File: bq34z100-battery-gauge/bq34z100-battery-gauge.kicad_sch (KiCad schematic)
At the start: 78 parts, among them J1 Conn_01x04, J10 Conn_01x10, J11 LED, J2 ALERT, J3 NTC, J4 LED_DISP, J5 BAT, J6 BAT, J7 LOAD, J8 LOAD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

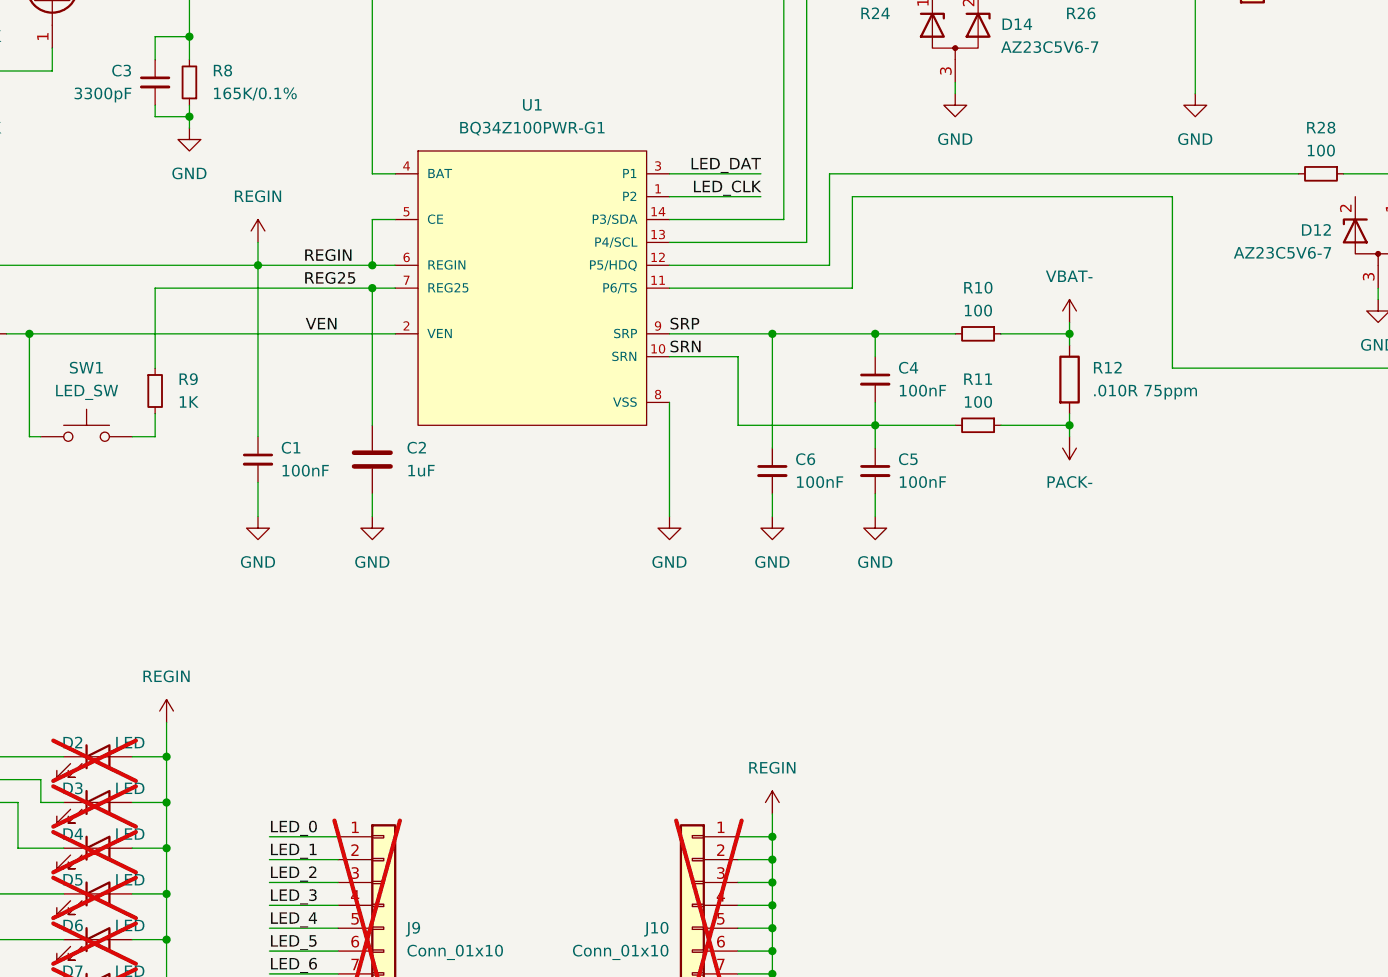
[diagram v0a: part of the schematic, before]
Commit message: Change Resistor to issabelenhurt, change mounting hole dimension
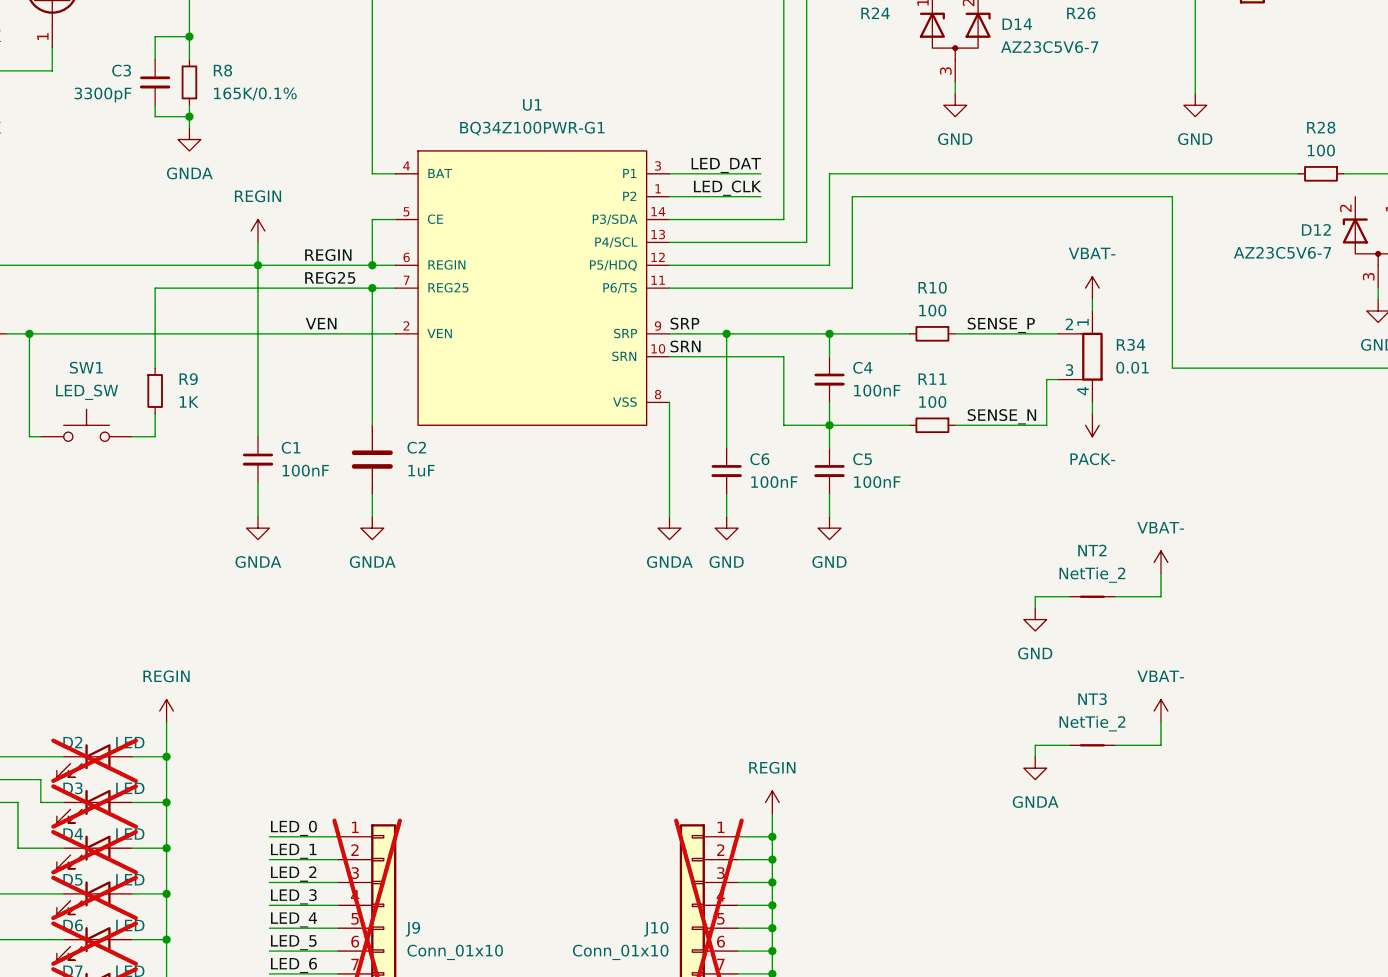
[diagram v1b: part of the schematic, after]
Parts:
- removed R12: .010R 75ppm, Resistor_SMD:R_2512_6332Metric, symbol Device:R
- added NT2, NT3: NetTie_2, NetTie:NetTie-2_SMD_Pad0.5mm, symbol Device:NetTie_2
- added R34: 0.01, shunt-resistor:Isabellenhuette-SMT-R010-1.0, symbol Device:R_Shunt
- J5, J6, J7, J8: footprint TerminalBlock_Wuerth:Wuerth_REDCUBE-THR_WP-THRBU_74650174_THR -> Plugin_terminal:square_terminal
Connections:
- net GND: now also NT2.1; no longer C1.2, C2.2, C3.2, R8.1, U1.8 (VSS)
- net PACK-: now also R34.4; no longer R11.1
- net VBAT-: now also NT2.2, NT3.2, R34.1; no longer R10.1
- new net GNDA: C1.2, C2.2, C3.2, NT3.1, R8.1, U1.8 (VSS)
- new net SENSE_N: R11.1, R34.3
- new net SENSE_P: R10.1, R34.2
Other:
- moved on the sheet: C4, C5, C6, R10, R11

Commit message: 1. Finished tracks, (need to verify grounding layer below battery tracks). 2. Added more literature document
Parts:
- removed R29: 1K, Resistor_SMD:R_0603_1608Metric, symbol Device:R_Small
- added TP1, TP2: TestPoint, TestPoint:TestPoint_Pad_D1.0mm, symbol Connector:TestPoint
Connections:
- net SENSE_N: now also TP2.1
- net SENSE_P: now also TP1.1
- net VEN: now also J4.1 (Pin_1); no longer J4.2 (Pin_2)
- net LED_SW: now reaches R9.2, SW1.2
- net LED_SW: now also J4.2 (Pin_2)
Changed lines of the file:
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@@
 	(paper "A4")
 	(junction
-		(at 246.38 72.39)
+		(at 123.19 60.96)
 		(diameter 0)
 		(color 0 0 0 0)
 	)
 	(junction
-		(at 123.19 60.96)
+		(at 36.83 26.67)
 		(diameter 0)
 		(color 0 0 0 0)
 	)
 	(junction
-		(at 36.83 26.67)
+		(at 167.64 124.46)
 		(diameter 0)
 		(color 0 0 0 0)
 	)
 	(junction
-		(at 167.64 124.46)
+		(at 99.06 77.47)
 		(diameter 0)
 		(color 0 0 0 0)
@@
 	(wire
 		(pts
+			(xy 196.85 130.81) (xy 205.74 130.81)
+		)
+		(stroke
+			(width 0)
+			(type default)
+		)
+	)
+	(wire
+		(pts
 			(xy 125.73 48.26) (xy 123.19 48.26)
 		)
@@
 	(wire
 		(pts
-			(xy 247.65 85.09) (xy 246.38 85.09)
+			(xy 247.65 85.09) (xy 238.76 85.09)
 		)
 		(stroke
@@
 	(wire
 		(pts
-			(xy 238.76 72.39) (xy 246.38 72.39)
+			(xy 238.76 72.39) (xy 247.65 72.39)
 		)
 		(stroke
@@
 	(wire
 		(pts
-			(xy 246.38 72.39) (xy 246.38 76.2)
-		)
-		(stroke
-			(width 0)
-			(type default)
-		)
-	)
-	(wire
-		(pts
 			(xy 168.91 22.86) (xy 176.53 22.86)
 		)
@@
 	(wire
 		(pts
+			(xy 196.85 123.19) (xy 205.74 123.19)
+		)
+		(stroke
+			(width 0)
+			(type default)
+		)
+	)
+	(wire
+		(pts
 			(xy 25.4 54.61) (xy 25.4 53.34)
 		)
@@
 	(wire
 		(pts
+			(xy 85.09 87.63) (xy 99.06 87.63)
+		)
+		(stroke
+			(width 0)
+			(type default)
+		)
+	)
+	(wire
+		(pts
 			(xy 21.59 104.14) (xy 31.75 104.14)
 		)
@@
 	(wire
 		(pts
-			(xy 246.38 81.28) (xy 246.38 85.09)
-		)
-		(stroke
-			(width 0)
-			(type default)
-		)
-	)
-	(wire
-		(pts
 			(xy 240.03 48.26) (xy 237.49 48.26)
 		)
@@
 	(wire
 		(pts
+			(xy 99.06 77.47) (xy 99.06 87.63)
+		)
+		(stroke
+			(width 0)
+			(type default)
+		)
+	)
+	(wire
+		(pts
 			(xy 31.75 123.19) (xy 30.48 123.19)
 		)
@@
 	(wire
 		(pts
-			(xy 246.38 72.39) (xy 247.65 72.39)
-		)
-		(stroke
-			(width 0)
-			(type default)
-		)
-	)
-	(wire
-		(pts
 			(xy 190.5 22.86) (xy 181.61 22.86)
 		)
@@
 		)
 	)
+	(label "LED_SW"
+		(at 85.09 87.63 0)
+		(fields_autoplaced yes)
+		(effects
+			(font
+				(size 1.27 1.27)
+			)
+			(justify left bottom)
+		)
+	)
 	(label "REG25"
 		(at 238.76 72.39 0)
@@
 		)
 	)
+	(label "LED_SW"
+		(at 238.76 85.09 0)
+		(fields_autoplaced yes)
+		(effects
+			(font
+				(size 1.27 1.27)
+			)
+			(justify left bottom)
+		)
+	)
 	(label "VEN"
 		(at 119.38 66.04 180)
@@
 		)
 	)
+	(label "SENSE_P"
+		(at 196.85 123.19 0)
+		(fields_autoplaced yes)
+		(effects
+			(font
+				(size 1.27 1.27)
+			)
+			(justify left bottom)
+		)
+	)
 	(label "LED_5"
 		(at 71.12 125.73 180)
@@
 		)
 	)
+	(label "SENSE_N"
+		(at 196.85 130.81 0)
+		(fields_autoplaced yes)
+		(effects
+			(font
+				(size 1.27 1.27)
+			)
+			(justify left bottom)
+		)
+	)
 	(label "LED_9"
 		(at 111.76 144.78 0)
@@
 	(symbol
 		(lib_id "Connector_Generic:Conn_01x02")
-		(at 252.73 85.09 0)
+		(at 252.73 87.63 0)
+		(mirror x)
 		(unit 1)
 		(exclude_from_sim no)
@@
 		(on_board yes)
 		(dnp no)
-		(fields_autoplaced yes)
 		(property "Reference" "J4"
-			(at 255.27 85.0899 0)
+			(at 255.27 87.6301 0)
 			(effects
 				(font
@@
 		)
 		(property "Value" "LED_DISP"
-			(at 255.27 87.6299 0)
+			(at 255.27 85.0901 0)
 			(effects
 				(font
@@
 		)
 		(property "Footprint" "Connector_JST:JST_XH_B2B-XH-A_1x02_P2.50mm_Vertical"
-			(at 252.73 85.09 0)
+			(at 252.73 87.63 0)
 			(effects
 				(font
@@
 		)
 		(property "Datasheet" "~"
-			(at 252.73 85.09 0)
+			(at 252.73 87.63 0)
 			(effects
 				(font
@@
 		)
 		(property "Description" "Generic connector, single row, 01x02, script generated (kicad-library-utils/schlib/autogen/connector/)"
-			(at 252.73 85.09 0)
+			(at 252.73 87.63 0)
 			(effects
 				(font
@@
 	)
 	(symbol
+		(lib_id "Connector:TestPoint")
+		(at 205.74 123.19 270)
+		(unit 1)
+		(exclude_from_sim no)
+		(in_bom yes)
+		(on_board yes)
+		(dnp no)
+		(fields_autoplaced yes)
+		(property "Reference" "TP1"
+			(at 210.82 121.9199 90)
+			(effects
+				(font
+					(size 1.27 1.27)
+				)
+				(justify left)
+			)
+		)
+		(property "Value" "TestPoint"
+			(at 210.82 124.4599 90)
+			(effects
+				(font
+					(size 1.27 1.27)
+				)
+				(justify left)
+			)
+		)
+		(property "Footprint" "TestPoint:TestPoint_Pad_D1.0mm"
+			(at 205.74 128.27 0)
+			(effects
+				(font
+					(size 1.27 1.27)
+				)
+				(hide yes)
+			)
+		)
+		(property "Datasheet" "~"
+			(at 205.74 128.27 0)
+			(effects
+				(font
+					(size 1.27 1.27)
+				)
+				(hide yes)
+			)
+		)
+		(property "Description" "test point"
+			(at 205.74 123.19 0)
+			(effects
+				(font
+					(size 1.27 1.27)
+				)
+				(hide yes)
+			)
+		)
+		(pin "1"
+		)
+		(instances
+			(project ""
+				(path "/1aa18a33-9f2d-4b3a-81cb-ca2880b63562"
+					(reference "TP1")
+					(unit 1)
+				)
+			)
+		)
+	)
+	(symbol
 		(lib_id "Device:NetTie_2")
 		(at 203.2 95.25 0)
@@
 	)
 	(symbol
+		(lib_id "Connector:TestPoint")
+		(at 205.74 130.81 270)
+		(unit 1)
+		(exclude_from_sim no)
+		(in_bom yes)
+		(on_board yes)
+		(dnp no)
+		(fields_autoplaced yes)
+		(property "Reference" "TP2"
+			(at 210.82 129.5399 90)
+			(effects
+				(font
+					(size 1.27 1.27)
+				)
+				(justify left)
+			)
+		)
+		(property "Value" "TestPoint"
+			(at 210.82 132.0799 90)
+			(effects
+				(font
+					(size 1.27 1.27)
+				)
+				(justify left)
+			)
+		)
+		(property "Footprint" "TestPoint:TestPoint_Pad_D1.0mm"
+			(at 205.74 135.89 0)
+			(effects
+				(font
+					(size 1.27 1.27)
+				)
+				(hide yes)
+			)
+		)
+		(property "Datasheet" "~"
+			(at 205.74 135.89 0)
+			(effects
+				(font
+					(size 1.27 1.27)
+				)
+				(hide yes)
+			)
+		)
+		(property "Description" "test point"
+			(at 205.74 130.81 0)
+			(effects
+				(font
+					(size 1.27 1.27)
+				)
+				(hide yes)
+			)
+		)
+		(pin "1"
+		)
+		(instances
+			(project "bq34z100-battery-gauge"
+				(path "/1aa18a33-9f2d-4b3a-81cb-ca2880b63562"
+					(reference "TP2")
+					(unit 1)
+				)
+			)
+		)
+	)
+	(symbol
 		(lib_id "Device:R_Small")
 		(at 74.93 41.91 180)
@@
 					(unit 1)
 				)
-			)
-		)
-	)
-	(symbol
-		(lib_id "Device:R_Small")
-		(at 246.38 78.74 0)
-		(unit 1)
-		(exclude_from_sim no)
-		(in_bom yes)
-		(on_board yes)
-		(dnp no)
-		(fields_autoplaced yes)
-		(property "Reference" "R29"
-			(at 248.92 77.4699 0)
-			(effects
-				(font
-					(size 1.27 1.27)
-				)
-				(justify left)
-			)
-		)
-		(property "Value" "1K"
-			(at 248.92 80.0099 0)
-			(effects
-				(font
-					(size 1.27 1.27)
-				)
-				(justify left)
-			)
-		)
-		(property "Footprint" "Resistor_SMD:R_0603_1608Metric"
-			(at 246.38 78.74 0)
-			(effects
-				(font
-					(size 1.27 1.27)
-				)
-				(hide yes)
-			)
-		)
-		(property "Datasheet" "~"
-			(at 246.38 78.74 0)
-			(effects
-				(font
-					(size 1.27 1.27)
-				)
-				(hide yes)
-			)
-		)
-		(property "Description" "Resistor, small symbol"
-			(at 246.38 78.74 0)
-			(effects
-				(font
-					(size 1.27 1.27)
-				)
-				(hide yes)
-			)
-		)
-		(pin "1"
-		)
-		(pin "2"
-		)
-		(instances
-			(project "bq34z100-battery-gauge"
-				(path "/1aa18a33-9f2d-4b3a-81cb-ca2880b63562"
-					(reference "R29")
-					(unit 1)
-				)
